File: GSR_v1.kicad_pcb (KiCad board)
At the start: 2 copper layers, 33.4 x 36 mm, 70 parts, among them IC1 AD5242BRUZ1M, J1 Micro_SD_Card_Det, P1 CONN_2, P2 CONN_2, P3 CONN_2, P4 CONN_2, Q1 DMP21D5UFB4-7B, U1 TPS63001, U2 LM324N, U3 NRF528XX-QFAA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

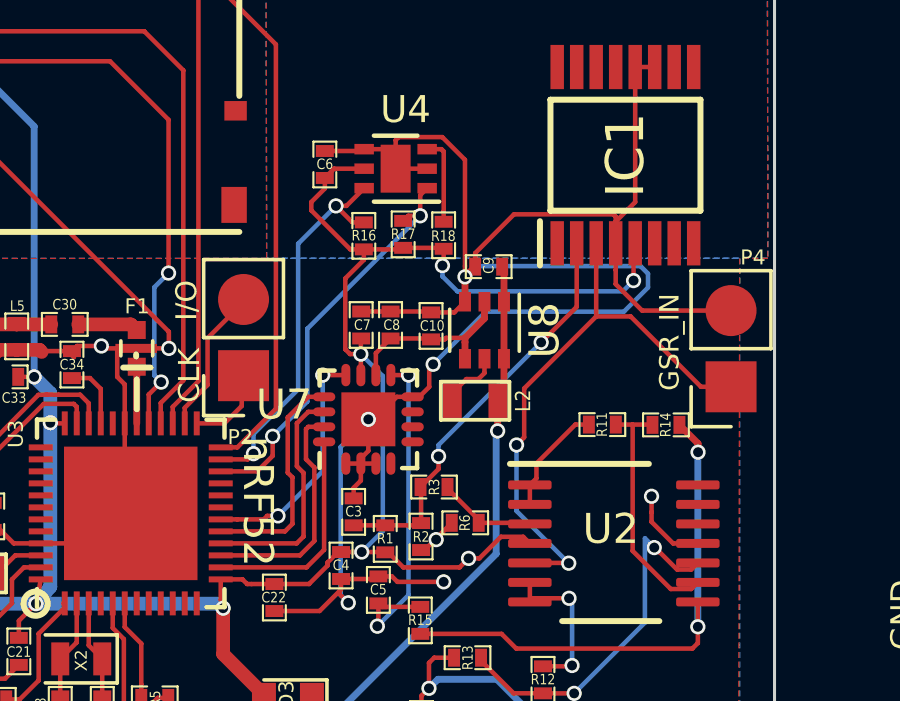
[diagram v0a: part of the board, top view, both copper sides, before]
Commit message: Fixed routing of AD5242.
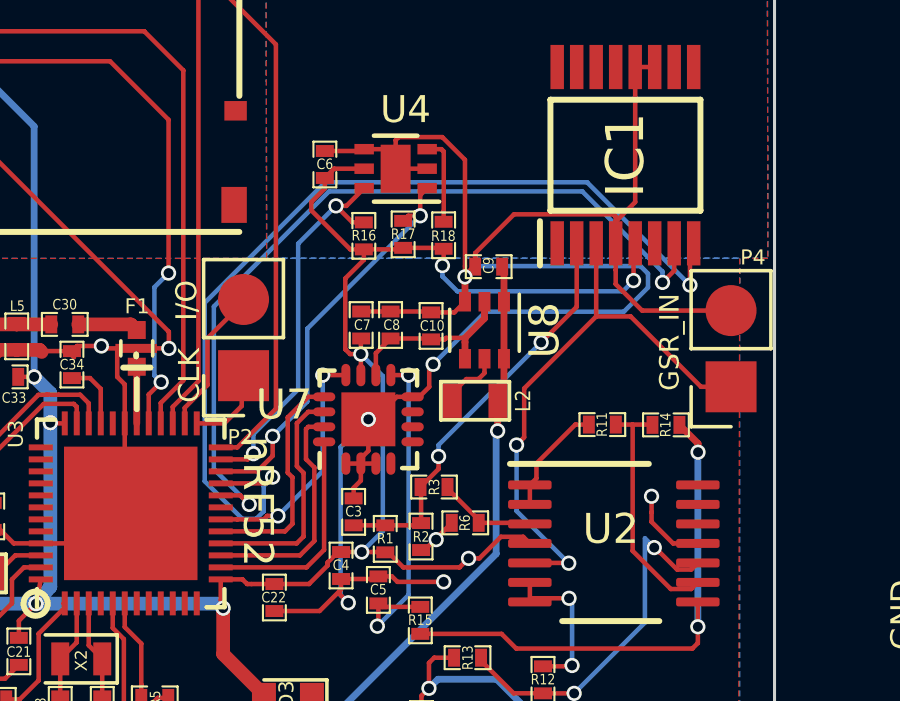
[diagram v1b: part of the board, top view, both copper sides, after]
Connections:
- U3 pad 20: Net-(U3-Pad20) -> /AD5242_SCL
- U3 pad 21: Net-(U3-Pad21) -> /AD5242_SDA
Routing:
- net /AD5242_SDA: track 0.00 -> 32.3 mm, vias 0 -> 2
- net /AD5242_SCL: track 0.00 -> 27.6 mm, vias 0 -> 2
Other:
- board text added: "nRF52-GSR (v2) Prototype 03/14/2019 Yeo GaTech BNE Lab"
- board text removed: "nRF52-GSR Prototype 01/09/2019 Yeo GaTech BNE Lab"

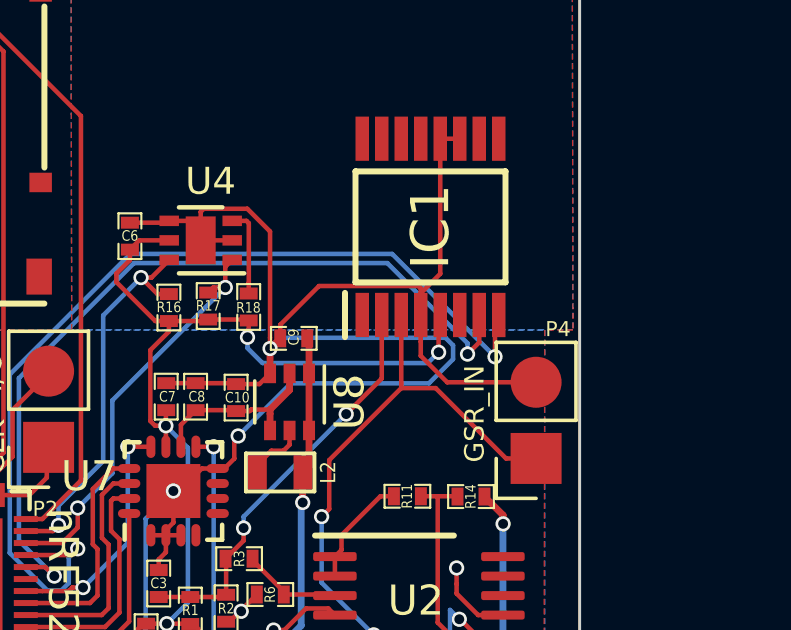
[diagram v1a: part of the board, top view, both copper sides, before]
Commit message: Fixed SHDN pin to VDD.
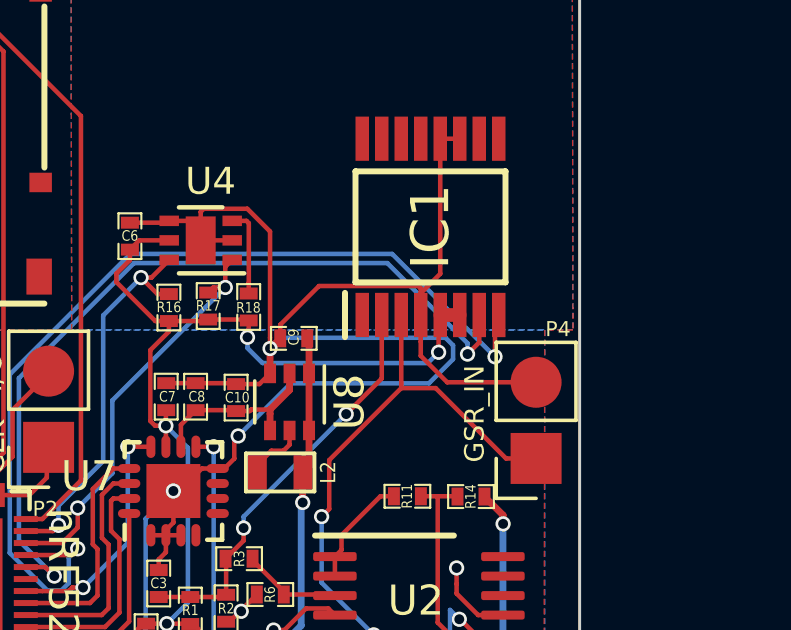
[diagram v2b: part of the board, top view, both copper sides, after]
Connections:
- IC1 pad 6: /AD5242_~SHDN -> DVDD
- U3 pad 20: /AD5242_SCL -> /AD5242_SDA
- U3 pad 21: /AD5242_SDA -> /AD5242_SCL
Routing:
- net DVDD: track 90.7 -> 91.3 mm

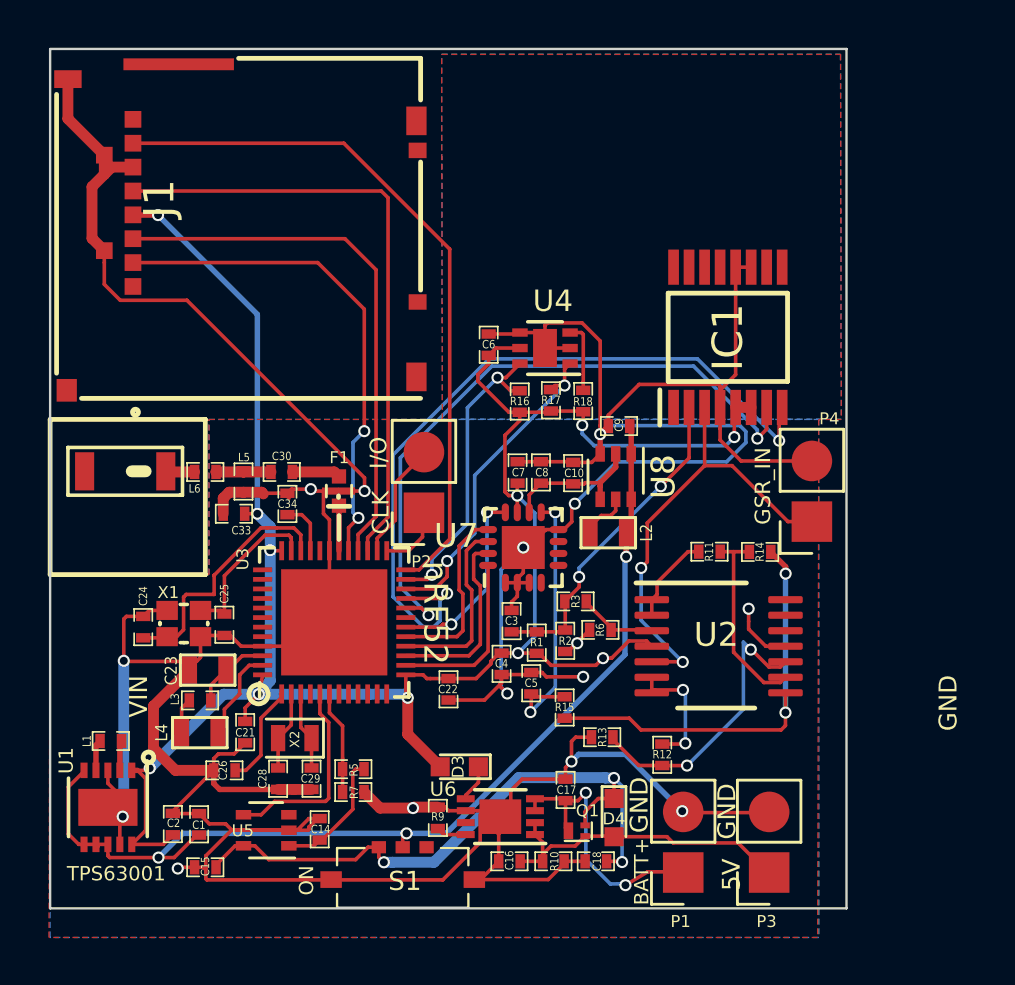
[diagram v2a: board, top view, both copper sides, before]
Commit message: Fixed footprint for ADS1220.
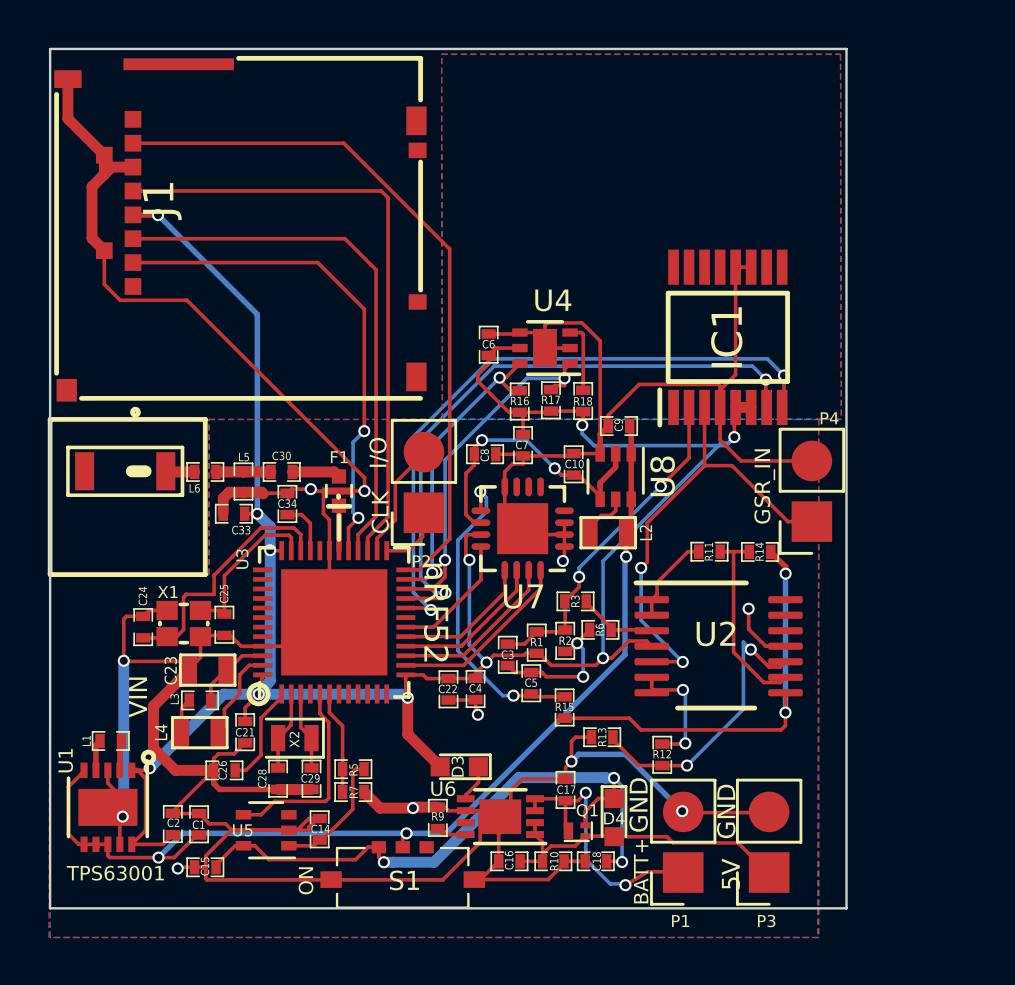
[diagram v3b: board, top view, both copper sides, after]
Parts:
- U7: footprint Package_DFN_QFN:QFN-16-1EP_3x3mm_P0.5mm_EP1.8x1.8mm -> pwrPad:QFN-16_EP_4.3x4.3_Pitch0.5mm
- moved C8 2.46 mm to (284.1, 127.0), turned to 0 degrees
- moved C4 1.52 mm to (283.7, 136.8)
- moved C3 1.42 mm to (285.1, 135.4), turned to 90 degrees
- moved C7 1.16 mm to (285.7, 126.6), turned to 270 degrees
- moved U7 0.79 mm to (285.7, 130.1), turned to 180 degrees
- moved C10 0.37 mm to (287.8, 127.4)
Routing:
- net DGND: track 228.4 -> 210.1 mm, vias 15 -> 13
- net DVDD: track 91.3 -> 98.3 mm
- net AVDD: track 6.11 -> 12.4 mm, vias 0 -> 2
- net /AD5242_SDA: track 32.3 -> 27.2 mm
- net /~DRDY: track 8.04 -> 5.36 mm, vias 2 -> 0
- net /ADC_AIN0: track 11.6 -> 13.4 mm
- net /DOUT: track 7.60 -> 5.83 mm
- net /AD5242_SCL: track 27.6 -> 26.0 mm
- net /DIN: track 7.79 -> 6.46 mm
- net /TMP_SCL: track 13.6 -> 14.8 mm
- net /SPI_SCLK: track 7.80 -> 7.11 mm
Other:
- board text added: "nRF52-GSR (v3) Prototype 03/31/2019 Yeo GaTech BNE Lab"
- board text removed: "nRF52-GSR (v2) Prototype 03/14/2019 Yeo GaTech BNE Lab"

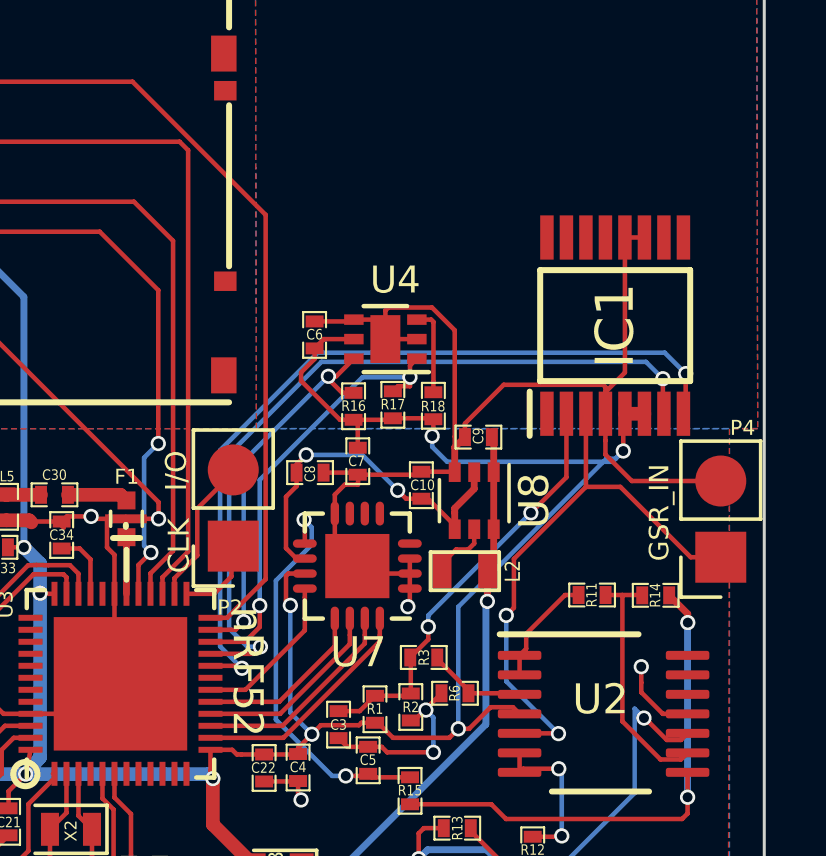
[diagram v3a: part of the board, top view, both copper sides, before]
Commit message: Finalized digital potentiometer ADC.
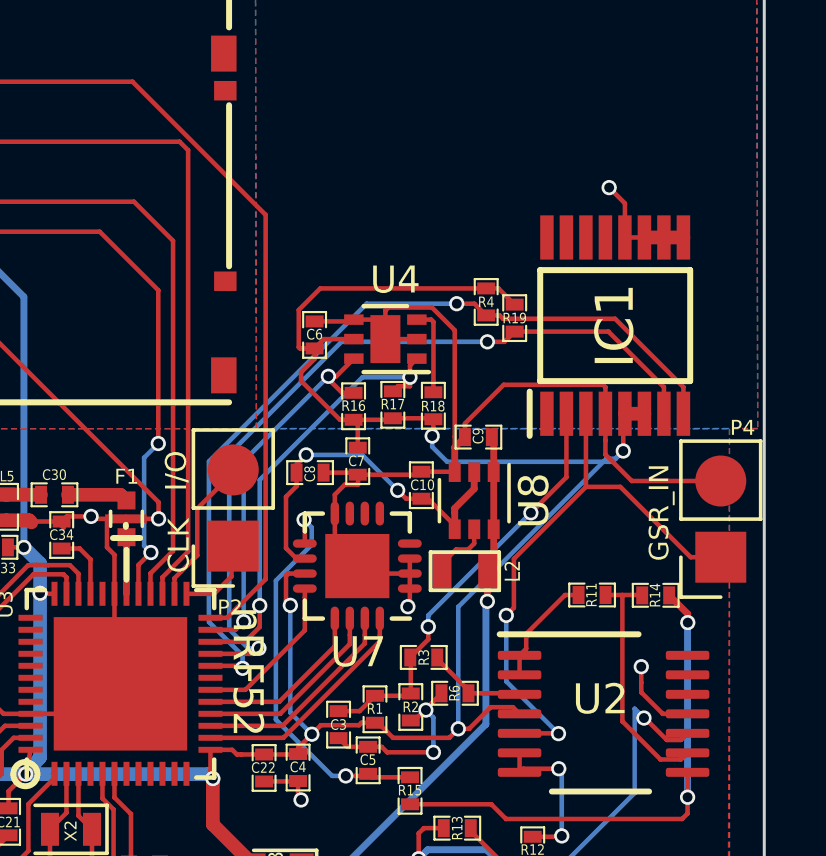
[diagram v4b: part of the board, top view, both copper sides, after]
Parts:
- added R19: 4.7k, SM0402, F.Cu at (290.9, 121.8)
- added R4: 4.7k, SM0402, F.Cu at (290.0, 121.3)
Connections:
- IC1 pad 10: Net-(IC1-Pad10) -> DGND
- IC1 pad 9: Net-(IC1-Pad9) -> DGND
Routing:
- net DVDD: track 98.3 -> 107.8 mm
- net DGND: track 210.1 -> 207.2 mm, vias 13 -> 14
- net /AD5242_SDA: track 27.2 -> 28.5 mm
- net /AD5242_SCL: track 26.0 -> 26.6 mm

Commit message: Updated schematic with new hex buffers for driving uSD Card.
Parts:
- removed R18: 4.7k, SM0402
- added C11: 0.1uF, SM0402, F.Cu at (290.7, 119.5)
- added D1: LED, LEDs:LED_0603, F.Cu at (294.3, 114.5)
- added R20: 1k, SM0402, F.Cu at (295.6, 114.6)
- added U9: 4050, CD74HC4050M:SOIC127P600X175-16N, F.Cu at (288.1, 114.3)
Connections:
- J1 pad 2: /DAT3_CS -> Net-(J1-Pad2)
- J1 pad 3: /CMD_MOSI -> Net-(J1-Pad3)
- J1 pad 5: /uSD_CLK -> Net-(J1-Pad5)
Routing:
- net Net-(J1-Pad2): track 0.00 -> 27.7 mm, vias 0 -> 2
- net Net-(J1-Pad5): track 0.00 -> 19.5 mm
- net Net-(J1-Pad3): track 0.00 -> 17.4 mm
- net DGND: track 207.2 -> 224.3 mm, vias 14 -> 15
- net DVDD: track 107.8 -> 119.3 mm, vias 11 -> 13
- net /DAT3_CS: track 21.1 -> 32.0 mm
- net Net-(D1-Pad2): track 0.00 -> 5.48 mm
- net Net-(D1-Pad1): track 0.00 -> 2.22 mm
- net /CMD_MOSI: track 22.8 -> 20.7 mm
- net /uSD_CLK: track 25.9 -> 24.9 mm, vias 0 -> 2
- net /DAT0_MISO: track 29.9 -> 29.2 mm, vias 0 -> 2

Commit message: Update bottom solder mask, and gerber files.
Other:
- board text added: "nRF52-GSR (v6) Prototype 05/02/2019 Yeo GaTech BNE Lab"
- board text removed: "nRF52-GSR (v3) Prototype 03/31/2019 Yeo GaTech BNE Lab"
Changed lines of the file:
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@@
     (34 B.Paste user)
     (35 F.Paste user hide)
-    (36 B.SilkS user hide)
+    (36 B.SilkS user)
     (37 F.SilkS user)
     (38 B.Mask user hide)
@@
   )
   (setup
-    (last_trace_width 0.152)
+    (last_trace_width 0.4572)
     (user_trace_width 0.152)
     (user_trace_width 0.229)
@@
   )
   (gr_line (start 269.9 127.673) (end 269.32 127.673) (angle 90) (layer F.SilkS) (width 0.5))
-  (gr_text "nRF52-GSR (v3) Prototype \n03/31/2019\nYeo GaTech BNE Lab" (at 273.36 141.38) (layer B.SilkS)
+  (gr_text "nRF52-GSR (v6) Prototype \n05/02/2019\nYeo GaTech BNE Lab" (at 274.35 140.075) (layer B.SilkS)
     (effects (font (size 0.762 0.762) (thickness 0.127)) (justify mirror))
   )
